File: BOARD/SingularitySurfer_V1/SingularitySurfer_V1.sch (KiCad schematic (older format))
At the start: 0 parts

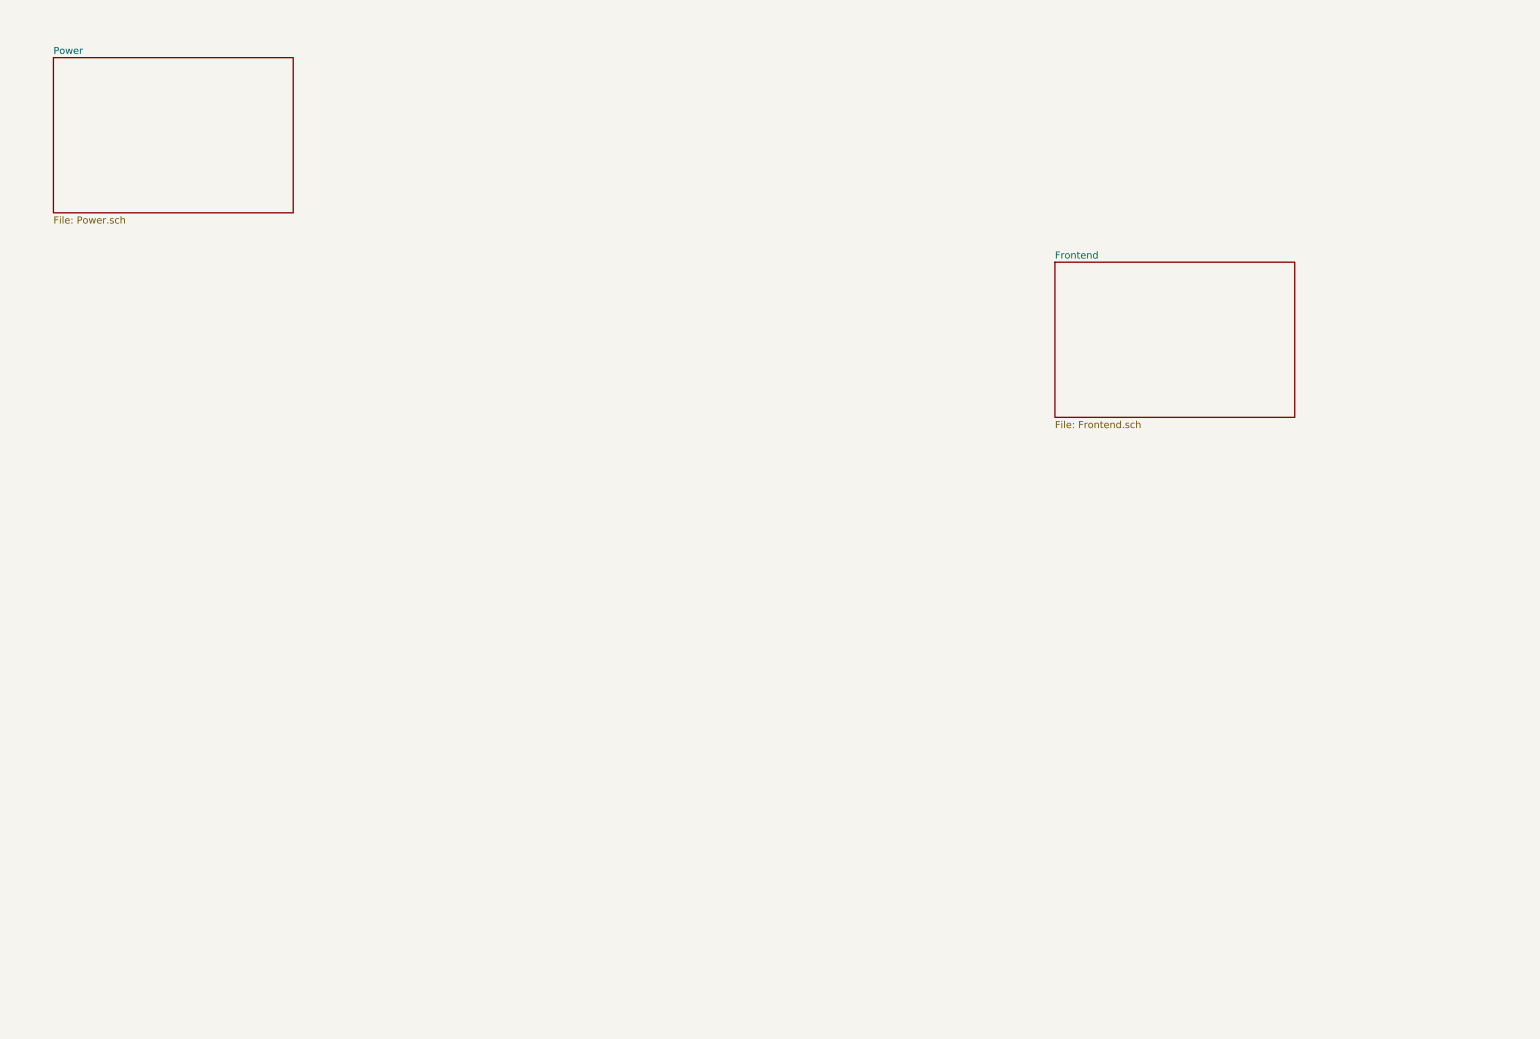
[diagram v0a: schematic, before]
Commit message: More work on final Schematic. Power, digital and output section close to final. No frontend yet.
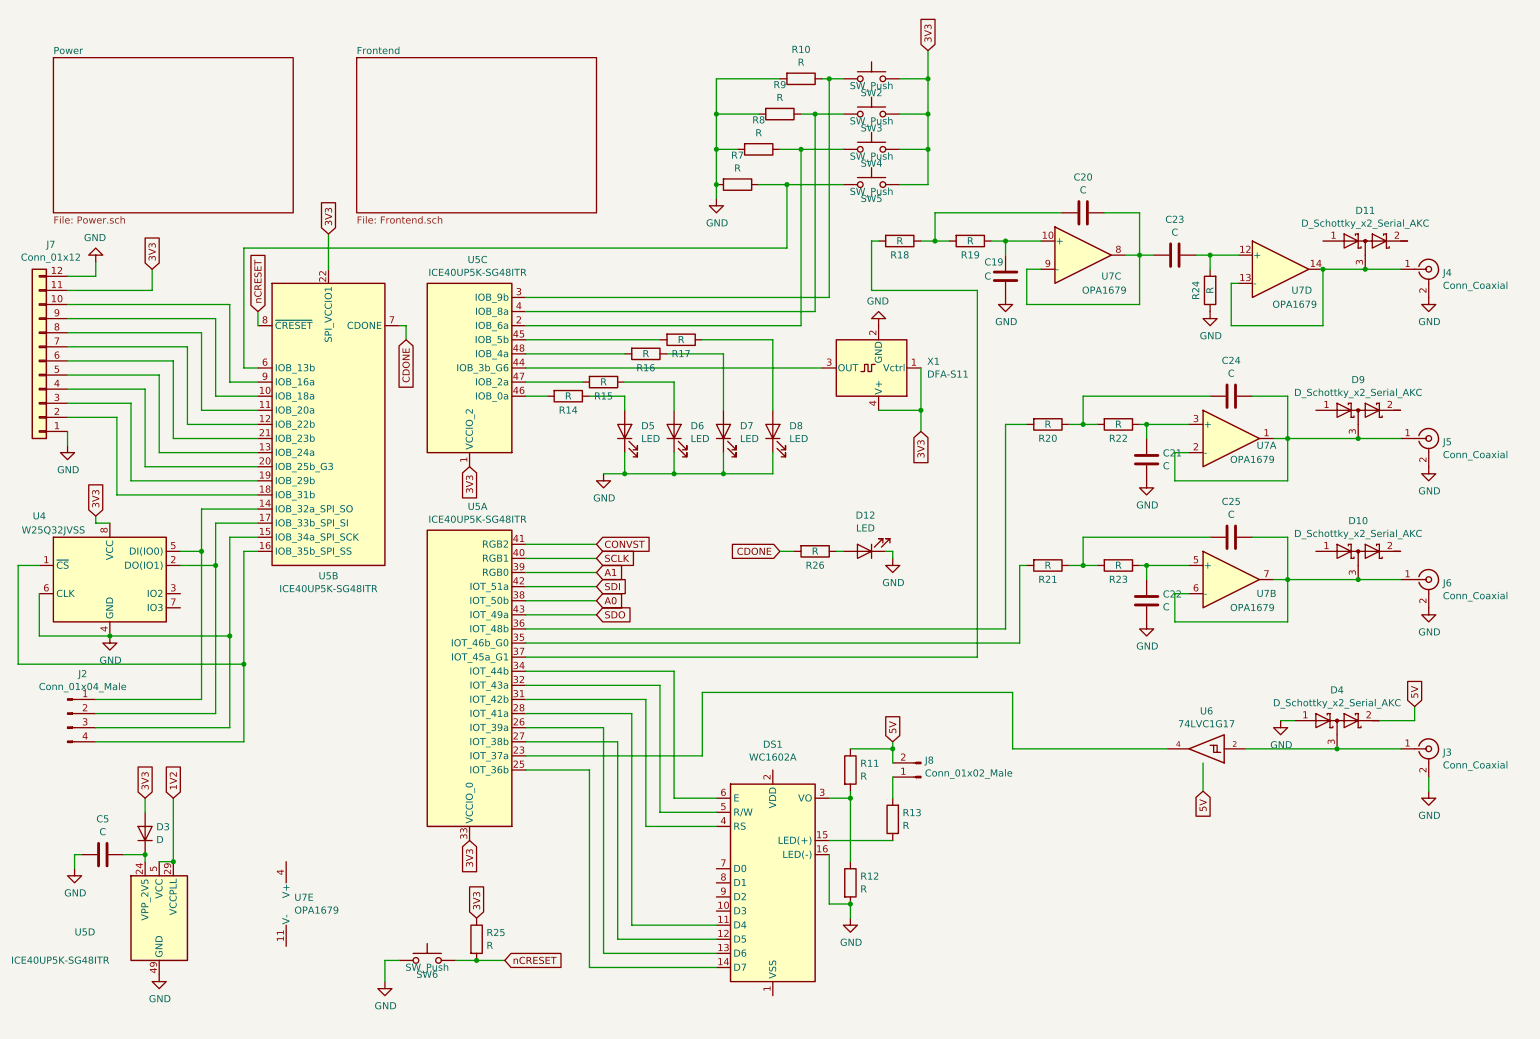
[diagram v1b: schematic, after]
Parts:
- added C19, C20, C21, C22, C23, C24, C25, C5: C, symbol Device:C
- added D10, D11, D4, D9: D_Schottky_x2_Serial_AKC, symbol Device:D_Schottky_x2_Serial_AKC
- added D12, D5, D6, D7, D8: LED, symbol Device:LED
- added D3: D, symbol Device:D
- added DS1: WC1602A, Display:WC1602A, symbol Display_Character:WC1602A
- added J2: Conn_01x04_Male, symbol Connector:Conn_01x04_Male
- added J3, J4, J5, J6: Conn_Coaxial, Connector_Coaxial:SMA_Molex_73251-2200_Horizontal, symbol Connector:Conn_Coaxial
- added J7: Conn_01x12, symbol Connector_Generic:Conn_01x12
- added J8: Conn_01x02_Male, symbol Connector:Conn_01x02_Male
- added R10, R11, R12, R13, R14, R15, R16, R17, R18, R19, R20, R21, R22, R23, R24, R25, R26, R7, R8, R9: R, symbol Device:R
- added SW2, SW3, SW4, SW5: SW_Push, Button_Switch_THT:SW_PUSH-12mm, symbol Switch:SW_Push
- added SW6: SW_Push, Button_Switch_THT:SW_PUSH_6mm, symbol Switch:SW_Push
- added U4: W25Q32JVSS, Package_SO:SOIC-8_5.23x5.23mm_P1.27mm, symbol Memory_Flash:W25Q32JVSS
- added U5: ICE40UP5K-SG48ITR, Package_DFN_QFN:QFN-48-1EP_7x7mm_P0.5mm_EP5.6x5.6mm, symbol FPGA_Lattice:ICE40UP5K-SG48ITR
- added U6: 74LVC1G17, Package_TO_SOT_SMD:SOT-23-5_HandSoldering, symbol 74xGxx:74LVC1G17
- added U7: OPA1679, Package_SO:SOIC-14_3.9x8.7mm_P1.27mm, symbol Amplifier_Operational:OPA1679
- added X1: DFA-S11, Oscillator:Oscillator_SMD_Fordahl_DFAS11-4Pin_7.0x5.0mm, symbol Oscillator:DFA-S11
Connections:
- new net: U5.23 (IOT_37a), U6.4
- new net: DS1.14 (D7), U5.25 (IOT_36b)
- new net: DS1.13 (D6), U5.26 (IOT_39a)
- new net: DS1.12 (D5), U5.27 (IOT_38b)
- new net: DS1.11 (D4), U5.28 (IOT_41a)
- new net: DS1.4 (RS), U5.31 (IOT_42b)
- new net: DS1.5 (R/W), U5.32 (IOT_43a)
- new net: DS1.6 (E), U5.34 (IOT_44b)
- new net: R21.2, U5.35 (IOT_46b_G0)
- new net: R20.2, U5.36 (IOT_48b)
- new net: R18.2, U5.37 (IOT_45a_G1)
- new net: J7.9 (Pin_9), U5.10 (IOB_18a)
- new net: J7.8 (Pin_8), U5.11 (IOB_20a)
- new net: J7.7 (Pin_7), U5.12 (IOB_22b)
- new net: J7.5 (Pin_5), U5.13 (IOB_24a)
- new net: J2.1 (Pin_1), U4.5 (DI(IO0)), U5.14 (IOB_32a_SPI_SO)
- new net: J2.4 (Pin_4), U4.1 (~CS), U5.16 (IOB_35b_SPI_SS)
- new net: J2.2 (Pin_2), U4.2 (DO(IO1)), U5.17 (IOB_33b_SPI_SI)
- new net: J7.2 (Pin_2), U5.18 (IOB_31b)
- new net: J7.3 (Pin_3), U5.19 (IOB_29b)
- new net: J7.4 (Pin_4), U5.20 (IOB_25b_G3)
- new net: J7.6 (Pin_6), U5.21 (IOB_23b)
- new net: R7.1, SW5.1, U5.6 (IOB_13b)
- new net: J7.10 (Pin_10), U5.9 (IOB_16a)
- new net: R8.1, SW4.1, U5.2 (IOB_6a)
- new net: R10.1, SW2.1, U5.3 (IOB_9b)
- new net: R9.1, SW3.1, U5.4 (IOB_8a)
- new net: U5.44 (IOB_3b_G6), X1.3 (OUT)
- new net: R17.2, U5.45 (IOB_5b)
- new net: R14.2, U5.46 (IOB_0a)
- new net: R15.2, U5.47 (IOB_2a)
- new net: R16.2, U5.48 (IOB_4a)
- new net: C5.1, D3.1 (K), U5.24 (VPP_2V5)
- new net: DS1.15 (LED(+)), R13.1
- new net: DS1.3 (VO), R11.2, R12.1
- new net: D4.3 (common), J3.1 (In), U6.2
- new net: J8.1 (Pin_1), R13.2
- new net: C24.1, D9.3 (common), J5.1 (In), U7.1, U7.2 (-)
- new net: C21.2, R22.1, U7.3 (+)
- new net: C22.2, R23.1, U7.5 (+)
- new net: C25.1, D10.3 (common), J6.1 (In), U7.6 (-), U7.7
- new net: C19.2, R19.1, U7.10 (+)
- new net: C20.1, C23.2, U7.8, U7.9 (-)
- new net: D11.3 (common), J4.1 (In), U7.13 (-), U7.14
- new net: C24.2, R20.1, R22.2
- new net: C25.2, R21.1, R23.2
- new net: C20.2, R18.1, R19.2
- new net: C23.1, R24.2, U7.12 (+)
- new net: D5.2 (A), R14.1
- new net: D6.2 (A), R15.1
- new net: D7.2 (A), R16.1
- new net: D8.2 (A), R17.1
- new net: D12.2 (A), R26.1
- new net 1V2: U5.29 (VCCPLL), U5.30 (VCC), U5.5 (VCC)
- new net 3V3: D3.2 (A), J7.11 (Pin_11), R25.1, SW2.2, SW3.2, SW4.2, SW5.2, U4.8 (VCC), U5.1 (VCCIO_2), U5.22 (SPI_VCCIO1), U5.33 (VCCIO_0), X1.1 (Vctrl), X1.4 (V+)
- new net A0: U5.38 (IOT_50b)
- new net A1: U5.39 (RGB0)
- new net CDONE: R26.2, U5.7 (CDONE)
- new net CONVST: U5.41 (RGB2)
- new net GND: C19.1, C21.1, C22.1, C5.2, D12.1 (K), D4.1 (A), D5.1 (K), D6.1 (K), D7.1 (K), D8.1 (K), DS1.16 (LED(-)), J2.3 (Pin_3), J3.2 (Ext), J4.2 (Ext), J5.2 (Ext), J6.2 (Ext), J7.1 (Pin_1), J7.12 (Pin_12), R10.2, R12.2, R24.1, R7.2, R8.2, R9.2, SW6.1, U4.4 (GND), U4.6 (CLK), U5.15 (IOB_34a_SPI_SCK), U5.49 (GND), U6.3 (GND), X1.2 (GND)
- new net SCLK: U5.40 (RGB1)
- new net SDI: U5.42 (IOT_51a)
- new net SDO: U5.43 (IOT_49a)
- new net VCC: D4.2 (K), J8.2 (Pin_2), R11.1, U6.5 (VCC)
- new net nCRESET: R25.2, SW6.2, U5.8 (~CRESET)

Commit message: Final Board schematic almost done and started on layout
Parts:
- C19, C20, C21, C22, C23, C24, C25: footprint (none) -> Capacitor_SMD:C_1206_3216Metric_Pad1.42x1.75mm_HandSolder
- C5: footprint (none) -> Capacitor_SMD:C_0805_2012Metric_Pad1.15x1.40mm_HandSolder
- D10, D11, D4, D9: footprint (none) -> Package_TO_SOT_SMD:SOT-23
- D12, D5, D6, D7, D8: footprint (none) -> LED_SMD:LED_0805_2012Metric_Pad1.15x1.40mm_HandSolder
- D3: footprint (none) -> Diode_SMD:D_SOD-123F
- J2: footprint (none) -> Connector_PinHeader_1.27mm:PinHeader_1x04_P1.27mm_Vertical
- J7: footprint (none) -> Connector_PinHeader_1.27mm:PinHeader_1x12_P1.27mm_Vertical
- J8: footprint (none) -> Connector_PinHeader_1.27mm:PinHeader_1x02_P1.27mm_Vertical
- R10, R11, R12, R13, R14, R15, R16, R17, R18, R19, R20, R21, R22, R23, R24, R25, R26, R7, R8, R9: footprint (none) -> Resistor_SMD:R_0805_2012Metric_Pad1.15x1.40mm_HandSolder
- renumbered SW3 to +1, SW5 to -1, SW4 to MENU1, SW2 to SET1001
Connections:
- net GND: now also C20.1, C24.1, C25.1, D10.1 (A), D11.1 (A), D9.1 (A); no longer J2.3 (Pin_3), U4.6 (CLK), U5.15 (IOB_34a_SPI_SCK)
- net VCC: now also D10.2 (K), D11.2 (K), D9.2 (K)
- net at J5.1 (In), U7.1, U7.2 (-): no longer C24.1, D9.3 (common)
- net at R23.1, U7.5 (+): now also C25.2; no longer C22.2
- net at D10.3 (common), J6.1 (In), U7.6 (-)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: no longer C25.1
- net at C23.2, U7.8, U7.9 (-): no longer C20.1
- net -8V: now reaches U7.11 (V-)
- net +8V: now reaches U7.4 (V+)
- net at J4.1 (In), U7.13 (-), U7.14: no longer D11.3 (common)
- net at R21.1, R23.2: now also C22.2; no longer C25.2
- new net: J2.3 (Pin_3), U4.6 (CLK), U5.15 (IOB_34a_SPI_SCK)
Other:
- moved on the sheet: C20, C24, D4, J2

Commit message: SignularitiSurfer final boar almost donegit status! Fuuuak this is getting rediculous...
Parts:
- J2: footprint Connector_PinHeader_1.27mm:PinHeader_1x04_P1.27mm_Vertical -> Connector_PinHeader_2.54mm:PinHeader_1x04_P2.54mm_Vertical
- J7: footprint Connector_PinHeader_1.27mm:PinHeader_1x12_P1.27mm_Vertical -> Connector_PinHeader_2.54mm:PinHeader_1x12_P2.54mm_Vertical
- J8: footprint Connector_PinHeader_1.27mm:PinHeader_1x02_P1.27mm_Vertical -> Connector_PinHeader_2.54mm:PinHeader_1x02_P2.54mm_Vertical
- U5: footprint Package_DFN_QFN:QFN-48-1EP_7x7mm_P0.5mm_EP5.6x5.6mm -> SingularitySurfer:QFN-48-1EP_7x7mm_P0.5mm_EP5.6x5.6mm
- renumbered SET1001 to SET1
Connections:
- net 3V3 is gone; now on net VCC: +1.2, -1.2, D3.2 (A), J7.11 (Pin_11), MENU1.2, R25.1, SET1.2, U4.8 (VCC), U5.1 (VCCIO_2), U5.22 (SPI_VCCIO1), U5.33 (VCCIO_0), X1.1 (Vctrl), X1.4 (V+)
- net VCC: no longer D10.2 (K), D11.2 (K), D4.2 (K), D9.2 (K), J8.2 (Pin_2), R11.1
- net 5V: now reaches DS1.2 (VDD)
- net 5V: now also D10.2 (K), D11.2 (K), D4.2 (K), D9.2 (K), J8.2 (Pin_2), R11.1
- net at J5.1 (In), U7.1, U7.2 (-): now also D9.3 (common)
- net at J4.1 (In), U7.13 (-), U7.14: now also D11.3 (common)
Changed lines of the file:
@@
 F 0 "U5" H 3693 3983 50  0000 C CNN
 F 1 "ICE40UP5K-SG48ITR" H 3693 4074 50  0000 C CNN
-F 2 "Package_DFN_QFN:QFN-48-1EP_7x7mm_P0.5mm_EP5.6x5.6mm" H 3750 3900 50  0001 C CNN
+F 2 "SingularitySurfer:QFN-48-1EP_7x7mm_P0.5mm_EP5.6x5.6mm" H 3750 3900 50  0001 C CNN
 F 3 "http://www.latticesemi.com/Products/FPGAandCPLD/iCE40Ultra" H 3350 6250 50  0001 C CNN
 	1    3750 5250
@@
 F 0 "U5" H 2750 2325 50  0000 C CNN
 F 1 "ICE40UP5K-SG48ITR" H 2750 2234 50  0000 C CNN
-F 2 "Package_DFN_QFN:QFN-48-1EP_7x7mm_P0.5mm_EP5.6x5.6mm" H 2750 2050 50  0001 C CNN
+F 2 "SingularitySurfer:QFN-48-1EP_7x7mm_P0.5mm_EP5.6x5.6mm" H 2750 2050 50  0001 C CNN
 F 3 "http://www.latticesemi.com/Products/FPGAandCPLD/iCE40Ultra" H 2350 4400 50  0001 C CNN
 	2    2750 3400
@@
 F 0 "U5" H 3693 2233 50  0000 C CNN
 F 1 "ICE40UP5K-SG48ITR" H 3693 2324 50  0000 C CNN
-F 2 "Package_DFN_QFN:QFN-48-1EP_7x7mm_P0.5mm_EP5.6x5.6mm" H 3750 1650 50  0001 C CNN
+F 2 "SingularitySurfer:QFN-48-1EP_7x7mm_P0.5mm_EP5.6x5.6mm" H 3750 1650 50  0001 C CNN
 F 3 "http://www.latticesemi.com/Products/FPGAandCPLD/iCE40Ultra" H 3350 4000 50  0001 C CNN
 	3    3750 3000
@@
 F 0 "U5" H 950 6800 50  0000 L CNN
 F 1 "ICE40UP5K-SG48ITR" H 500 6600 50  0000 L CNN
-F 2 "Package_DFN_QFN:QFN-48-1EP_7x7mm_P0.5mm_EP5.6x5.6mm" H 1550 5550 50  0001 C CNN
+F 2 "SingularitySurfer:QFN-48-1EP_7x7mm_P0.5mm_EP5.6x5.6mm" H 1550 5550 50  0001 C CNN
 F 3 "http://www.latticesemi.com/Products/FPGAandCPLD/iCE40Ultra" H 1150 7900 50  0001 C CNN
 	4    1550 6900
@@
 $EndComp
 $Comp
-L Switch:SW_Push SET1001
+L Switch:SW_Push SET1
 U 1 1 5D91CE17
 P 6600 950
-F 0 "SET1001" H 6600 850 50  0000 C CNN
+F 0 "SET1" H 6600 850 50  0000 C CNN
 F 1 "SW_Push" H 6600 900 50  0000 C CNN
 F 2 "Button_Switch_THT:SW_PUSH-12mm" H 6600 1150 50  0001 C CNN
@@
 F 0 "J2" H 1008 5831 50  0000 C CNN
 F 1 "Conn_01x04_Male" H 1008 5740 50  0000 C CNN
-F 2 "Connector_PinHeader_1.27mm:PinHeader_1x04_P1.27mm_Vertical" H 900 5550 50  0001 C CNN
+F 2 "Connector_PinHeader_2.54mm:PinHeader_1x04_P2.54mm_Vertical" H 900 5550 50  0001 C CNN
 F 3 "~" H 900 5550 50  0001 C CNN
 	1    900  5550
@@
 Wire Wire Line
 	5400 5300 7600 5300
-Text GLabel 8950 6000 3    50   Input ~ 0
-5V
 Wire Wire Line
 	8950 6000 8950 5800
@@
 F 0 "J7" H 618 2125 50  0000 C CNN
 F 1 "Conn_01x12" H 618 2216 50  0000 C CNN
-F 2 "Connector_PinHeader_1.27mm:PinHeader_1x12_P1.27mm_Vertical" H 700 2950 50  0001 C CNN
+F 2 "Connector_PinHeader_2.54mm:PinHeader_1x12_P2.54mm_Vertical" H 700 2950 50  0001 C CNN
 F 3 "~" H 700 2950 50  0001 C CNN
 	1    700  2950
@@
 F 0 "J8" H 6922 5782 50  0000 R CNN
 F 1 "Conn_01x02_Male" H 6922 5873 50  0000 R CNN
-F 2 "Connector_PinHeader_1.27mm:PinHeader_1x02_P1.27mm_Vertical" H 6950 5900 50  0001 C CNN
+F 2 "Connector_PinHeader_2.54mm:PinHeader_1x02_P2.54mm_Vertical" H 6950 5900 50  0001 C CNN
 F 3 "~" H 6950 5900 50  0001 C CNN
 	1    6950 5900
@@
 	7750 1900 7650 1900
 Wire Wire Line
-	9550 3500 10350 3500
-Wire Wire Line
-	9800 2300 10350 2300
+	9550 3500 10050 3500
+Wire Wire Line
+	9800 2300 10250 2300
 $Comp
 L Device:D_Schottky_x2_Serial_AKC D10
@@
 Wire Wire Line
 	2050 5150 2050 5650
+Wire Wire Line
+	6450 5700 5900 5700
+Wire Wire Line
+	5900 5700 5900 5850
+Connection ~ 6450 5700
+Text GLabel 8950 6000 3    50   Input ~ 0
+3V3
+Connection ~ 10050 4500
+Connection ~ 10050 3500
+Wire Wire Line
+	10050 3500 10350 3500
+Connection ~ 10250 2300
+Wire Wire Line
+	10250 2300 10350 2300
 $EndSCHEMATC

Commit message: Final board done, plotted and in production. Started on LCD driver, already working with scrolling HI :)
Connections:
- net GND: now also DS1.1 (VSS)
- no-connect marks 0 -> 6
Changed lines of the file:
@@
 Wire Wire Line
 	10800 2100 10550 2100
-Text GLabel 2450 6500 1    50   Input ~ 0
-+8V
-Text GLabel 2450 7100 3    50   Input ~ 0
--8V
 Connection ~ 10050 5700
 Wire Wire Line
@@
 Wire Wire Line
 	10250 2300 10350 2300
+NoConn ~ 5500 6550
+NoConn ~ 5500 6650
+NoConn ~ 5500 6750
+NoConn ~ 5500 6850
+$Comp
+L power:GND #PWR0164
+U 1 1 5D9CB423
+P 5900 7450
+F 0 "#PWR0164" H 5900 7200 50  0001 C CNN
+F 1 "GND" H 5905 7277 50  0000 C CNN
+F 2 "" H 5900 7450 50  0001 C CNN
+F 3 "" H 5900 7450 50  0001 C CNN
+	1    5900 7450
+	1    0    0    -1
+$EndComp
+NoConn ~ 1700 4600
+NoConn ~ 1700 4700
+Text GLabel 2450 6500 1    50   Input ~ 0
++8V
+Text GLabel 2450 7100 3    50   Input ~ 0
+-8V
 $EndSCHEMATC
